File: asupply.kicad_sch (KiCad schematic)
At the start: 122 parts, among them U10 LT3081xDF, U11 LT3042xMSE, U12 LT3045xMSE, U13 LT3042xMSE, U14 LT3094xMSE, U15 LT3042xMSE, U16 LT3045xMSE, U9 LTC3261

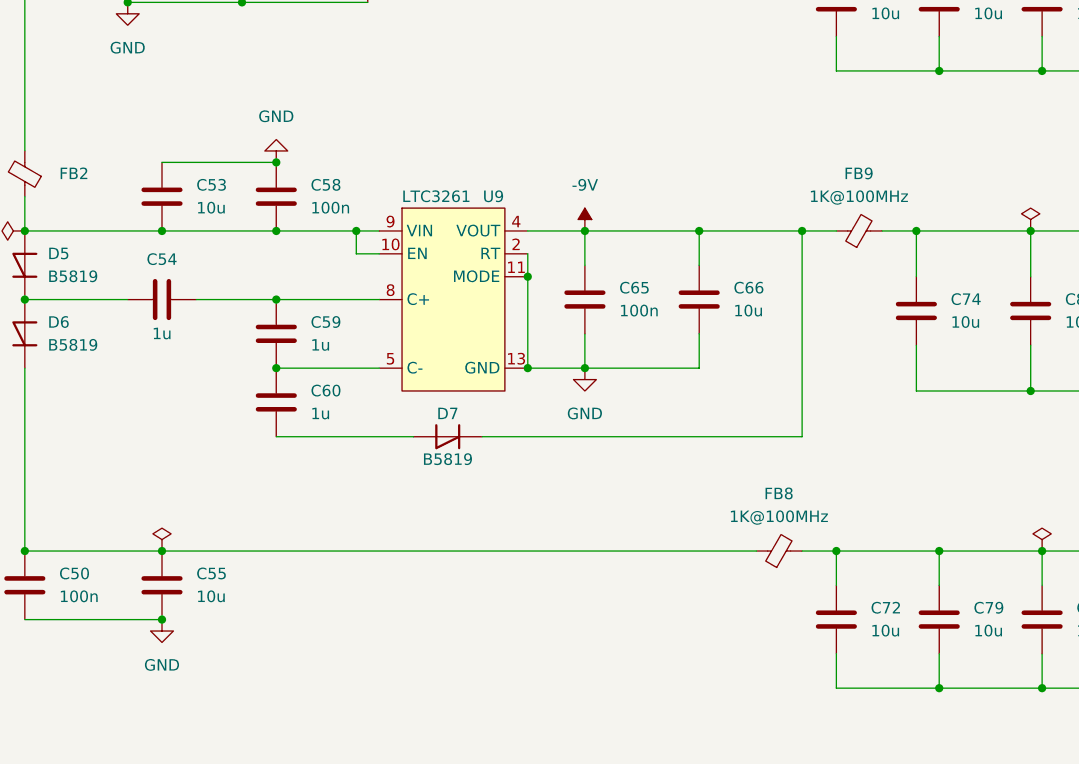
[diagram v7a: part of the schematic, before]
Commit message: sch, pcb: Replace FB of -6V +15V LDO with inductor - Build a Pi LPF on the input side
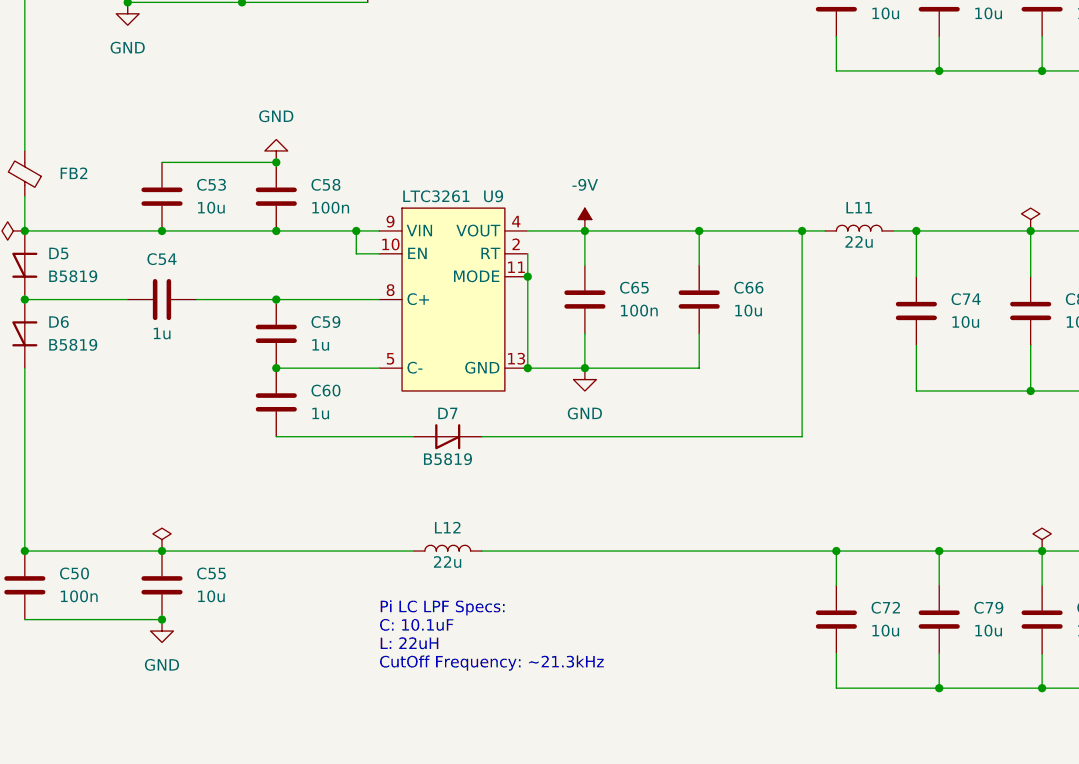
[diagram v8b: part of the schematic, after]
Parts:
- removed FB8, FB9: 1K@100MHz, Inductor_SMD:L_1210_3225Metric, symbol Device:FerriteBead_Small
- added L11, L12: 22u, Inductor_SMD:L_1210_3225Metric, symbol Device:L
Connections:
- net -9V: now also L11.1
- net at C72.1, C79.1, C86.1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: now also L12.2
- net at C50.1, C55.1, D6.1 (K): now also L12.1
- net at C74.1, C81.1, U14.1 (IN)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: now also L11.2
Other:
- note added: "Pi LC LPF Specs: C: 10.1uF L: 22uH CutOff Frequency: ~21.3kHz"
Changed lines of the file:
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@@
   (junction (at 306.705 107.95) (diameter 0) (color 0 0 0 0)
   )
+  (junction (at 160.02 201.93) (diameter 0) (color 0 0 0 0)
+  )
   (junction (at 99.06 44.45) (diameter 0) (color 0 0 0 0)
   )
@@
   (junction (at 281.94 219.71) (diameter 0) (color 0 0 0 0)
   )
-  (junction (at 160.02 201.93) (diameter 0) (color 0 0 0 0)
-  )
   (junction (at 186.69 59.69) (diameter 0) (color 0 0 0 0)
   )
@@
   (junction (at 208.28 91.44) (diameter 0) (color 0 0 0 0)
   )
-  (junction (at 172.72 201.93) (diameter 0) (color 0 0 0 0)
-  )
   (junction (at 208.28 153.67) (diameter 0) (color 0 0 0 0)
   )
@@
   (junction (at 129.54 217.17) (diameter 0) (color 0 0 0 0)
   )
+  (junction (at 172.72 201.93) (diameter 0) (color 0 0 0 0)
+  )
   (junction (at 236.22 138.43) (diameter 0) (color 0 0 0 0)
   )
@@
     (stroke (width 0) (type default))
   )
-  (wire (pts (xy 160.02 237.49) (xy 163.83 237.49))
+  (wire (pts (xy 124.46 237.49) (xy 163.83 237.49))
     (stroke (width 0) (type default))
   )
@@
     (stroke (width 0) (type default))
   )
+  (wire (pts (xy 170.18 201.93) (xy 172.72 201.93))
+    (stroke (width 0) (type default))
+  )
   (wire (pts (xy 186.69 80.01) (xy 186.69 76.2))
     (stroke (width 0) (type default))
@@
     (stroke (width 0) (type default))
   )
+  (wire (pts (xy 73.66 237.49) (xy 88.9 237.49))
+    (stroke (width 0) (type default))
+  )
   (wire (pts (xy 73.66 198.12) (xy 73.66 201.93))
     (stroke (width 0) (type default))
@@
     (stroke (width 0) (type default))
   )
-  (wire (pts (xy 73.66 237.49) (xy 88.9 237.49))
-    (stroke (width 0) (type default))
-  )
   (wire (pts (xy 175.26 168.91) (xy 186.69 168.91))
     (stroke (width 0) (type default))
@@
     (stroke (width 0) (type default))
   )
-  (wire (pts (xy 168.91 201.93) (xy 172.72 201.93))
-    (stroke (width 0) (type default))
-  )
   (wire (pts (xy 186.69 48.26) (xy 186.69 44.45))
     (stroke (width 0) (type default))
@@
     (stroke (width 0) (type default))
   )
-  (wire (pts (xy 160.02 201.93) (xy 163.83 201.93))
-    (stroke (width 0) (type default))
-  )
   (wire (pts (xy 267.97 237.49) (xy 281.94 237.49))
     (stroke (width 0) (type default))
@@
     (stroke (width 0) (type default))
   )
+  (wire (pts (xy 88.9 237.49) (xy 116.84 237.49))
+    (stroke (width 0) (type default))
+  )
   (wire (pts (xy 175.26 91.44) (xy 186.69 91.44))
     (stroke (width 0) (type default))
@@
     (stroke (width 0) (type default))
   )
+  (wire (pts (xy 160.02 201.93) (xy 162.56 201.93))
+    (stroke (width 0) (type default))
+  )
   (wire (pts (xy 281.94 214.63) (xy 281.94 219.71))
     (stroke (width 0) (type default))
@@
     (stroke (width 0) (type default))
   )
-  (wire (pts (xy 88.9 237.49) (xy 154.94 237.49))
-    (stroke (width 0) (type default))
-  )
   (wire (pts (xy 207.01 113.03) (xy 241.3 113.03))
     (stroke (width 0) (type default))
@@
     (stroke (width 0) (type default))
   )
+  (text "Pi LC LPF Specs:\nC: 10.1uF\nL: 22uH\nCutOff Frequency: ~21.3kHz"
+    (at 113.03 250.825 0)
+    (effects (font (size 1.27 1.27)) (justify left bottom))
+  )
   (hierarchical_label "LD_EN" (shape input) (at 230.505 107.95 180) (fields_autoplaced)
     (effects (font (size 1.27 1.27)) (justify right))
@@
     )
   )
-  (symbol (lib_id "Device:FerriteBead_Small") (at 166.37 201.93 90) (unit 1)
-    (in_bom yes) (on_board yes) (dnp no) (fields_autoplaced)
-    (property "Reference" "FB9" (at 166.3319 195.58 90)
-      (effects (font (size 1.27 1.27)))
-    )
-    (property "Value" "1K@100MHz" (at 166.3319 198.12 90)
-      (effects (font (size 1.27 1.27)))
-    )
-    (property "Footprint" "Inductor_SMD:L_1210_3225Metric" (at 166.37 203.708 90)
-      (effects (font (size 1.27 1.27)) hide)
-    )
-    (property "Datasheet" "~" (at 166.37 201.93 0)
-      (effects (font (size 1.27 1.27)) hide)
-    )
-    (property "MFR_PN" "FBMH3225HM102NT" (at 166.37 201.93 0)
-      (effects (font (size 1.27 1.27)) hide)
-    )
-    (property "MFR_PN_ALT" "FBMH3225HM102NTV" (at 166.37 201.93 0)
-      (effects (font (size 1.27 1.27)) hide)
-    )
-    (pin "1")
-    (pin "2")
-    (instances
-      (project "kirdy"
-        (path "/88da1dd8-9274-4b55-84fb-90006c9b6e8f/ce1698cd-b99b-406e-8c10-58c1e24b12e9"
-          (reference "FB9") (unit 1)
-        )
-      )
-    )
-  )
   (symbol (lib_id "power:+3.3VA") (at 346.71 184.785 270) (unit 1)
     (in_bom yes) (on_board yes) (dnp no)
@@
     )
   )
+  (symbol (lib_id "Device:L") (at 120.65 237.49 90) (unit 1)
+    (in_bom yes) (on_board yes) (dnp no)
+    (property "Reference" "L12" (at 120.65 234.95 90)
+      (effects (font (size 1.27 1.27)))
+    )
+    (property "Value" "22u" (at 120.65 238.76 90)
+      (effects (font (size 1.27 1.27)))
+    )
+    (property "Footprint" "Inductor_SMD:L_1210_3225Metric" (at 120.65 237.49 0)
+      (effects (font (size 1.27 1.27)) hide)
+    )
+    (property "Datasheet" "https://www.mouser.hk/datasheet/2/396/LSQ02_e-3082146.pdf" (at 120.65 237.49 0)
+      (effects (font (size 1.27 1.27)) hide)
+    )
+    (property "MFR_PN" "C3225T220KR" (at 120.65 237.49 90)
+      (effects (font (size 1.27 1.27)) hide)
+    )
+    (property "MFR_PN_ALT" "LSQPA322525T220KR" (at 120.65 237.49 90)
+      (effects (font (size 1.27 1.27)) hide)
+    )
+    (pin "1")
+    (pin "2")
+    (instances
+      (project "kirdy"
+        (path "/88da1dd8-9274-4b55-84fb-90006c9b6e8f/ce1698cd-b99b-406e-8c10-58c1e24b12e9"
+          (reference "L12") (unit 1)
+        )
+      )
+    )
+  )
   (symbol (lib_id "power:GND") (at 372.11 102.87 180) (unit 1)
     (in_bom yes) (on_board yes) (dnp no)
@@
     )
   )
-  (symbol (lib_id "Device:FerriteBead_Small") (at 157.48 237.49 90) (unit 1)
-    (in_bom yes) (on_board yes) (dnp no) (fields_autoplaced)
-    (property "Reference" "FB8" (at 157.4419 231.14 90)
-      (effects (font (size 1.27 1.27)))
-    )
-    (property "Value" "1K@100MHz" (at 157.4419 233.68 90)
-      (effects (font (size 1.27 1.27)))
-    )
-    (property "Footprint" "Inductor_SMD:L_1210_3225Metric" (at 157.48 239.268 90)
-      (effects (font (size 1.27 1.27)) hide)
-    )
-    (property "Datasheet" "~" (at 157.48 237.49 0)
-      (effects (font (size 1.27 1.27)) hide)
-    )
-    (property "MFR_PN" "FBMH3225HM102NT" (at 157.48 237.49 0)
-      (effects (font (size 1.27 1.27)) hide)
-    )
-    (property "MFR_PN_ALT" "FBMH3225HM102NTV" (at 157.48 237.49 0)
-      (effects (font (size 1.27 1.27)) hide)
-    )
-    (pin "1")
-    (pin "2")
-    (instances
-      (project "kirdy"
-        (path "/88da1dd8-9274-4b55-84fb-90006c9b6e8f/ce1698cd-b99b-406e-8c10-58c1e24b12e9"
-          (reference "FB8") (unit 1)
-        )
-      )
-    )
-  )
   (symbol (lib_id "power:+5VA") (at 146.05 168.91 90) (unit 1)
     (in_bom yes) (on_board yes) (dnp no) (fields_autoplaced)
@@
         )
       )
+    )
+  )
+  (symbol (lib_id "Device:L") (at 166.37 201.93 90) (unit 1)
+    (in_bom yes) (on_board yes) (dnp no)
+    (property "Reference" "L11" (at 166.37 199.39 90)
+      (effects (font (size 1.27 1.27)))
+    )
+    (property "Value" "22u" (at 166.37 203.2 90)
+      (effects (font (size 1.27 1.27)))
+    )
+    (property "Footprint" "Inductor_SMD:L_1210_3225Metric" (at 166.37 201.93 0)
+      (effects (font (size 1.27 1.27)) hide)
+    )
+    (property "Datasheet" "https://www.mouser.hk/datasheet/2/396/LSQ02_e-3082146.pdf" (at 166.37 201.93 0)
+      (effects (font (size 1.27 1.27)) hide)
+    )
+    (property "MFR_PN" "C3225T220KR" (at 166.37 201.93 90)
+      (effects (font (size 1.27 1.27)) hide)
+    )
+    (property "MFR_PN_ALT" "LSQPA322525T220KR" (at 166.37 201.93 90)
+      (effects (font (size 1.27 1.27)) hide)
+    )
+    (pin "1")
+    (pin "2")
+    (instances
+      (project "kirdy"
+        (path "/88da1dd8-9274-4b55-84fb-90006c9b6e8f/ce1698cd-b99b-406e-8c10-58c1e24b12e9"
+          (reference "L11") (unit 1)
+        )
+      )
